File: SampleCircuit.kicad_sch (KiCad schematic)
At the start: 36 parts, among them J1 24V INPUT, J2 12V TEST, J3 5V TEST, J4 3.3V TEST, J5 SPEAKER, U1 LMZM23601SILR, U2 ESP32-S3-WROOM-1, U5 LMZM23601SILR, U5 NS4168, U6 LMZM23601SILR, U6 MicroSD

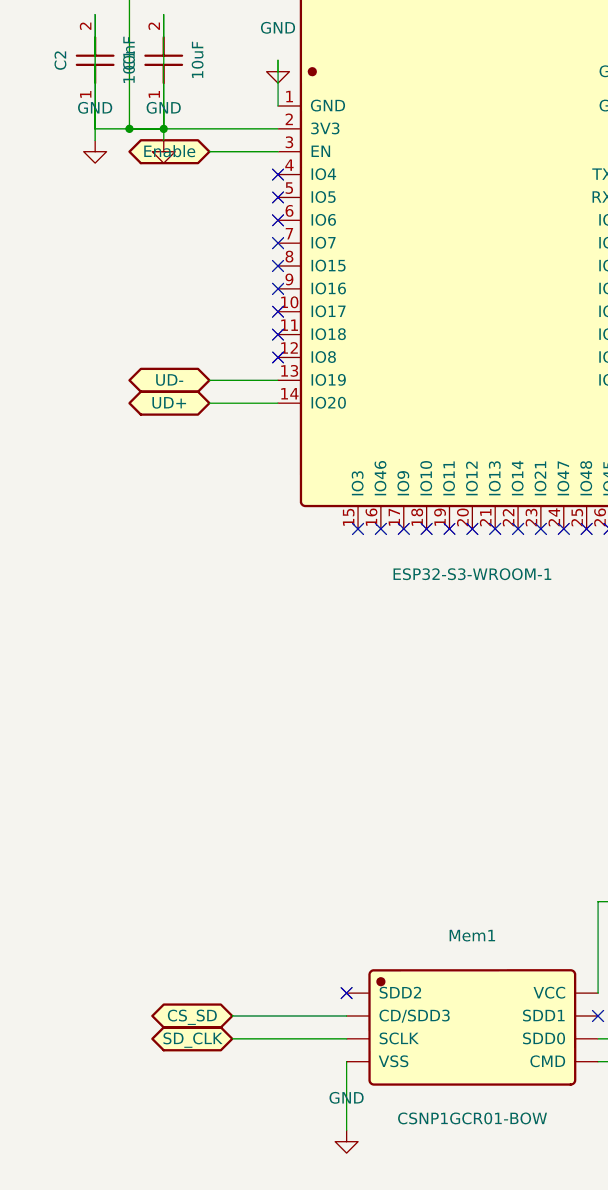
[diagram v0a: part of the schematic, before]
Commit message: Fix ESP32 GPIO wiring and flash chip select separation
- Add CS_FLASH port symbol to Ports.kicad_sym
- Map 9 ESP32 GPIO to ports: I2S (IO4-IO6), AMP_EN (IO7),
  SPI (IO15-IO18), CS_FLASH (IO8)
- Change flash template from CS_SD to CS_FLASH for separate
  chip select lines between flash and SD card
- Regenerate schematic with all signal connections verified

Co-Authored-By: Claude Opus 4.6 <noreply@anthropic.com>
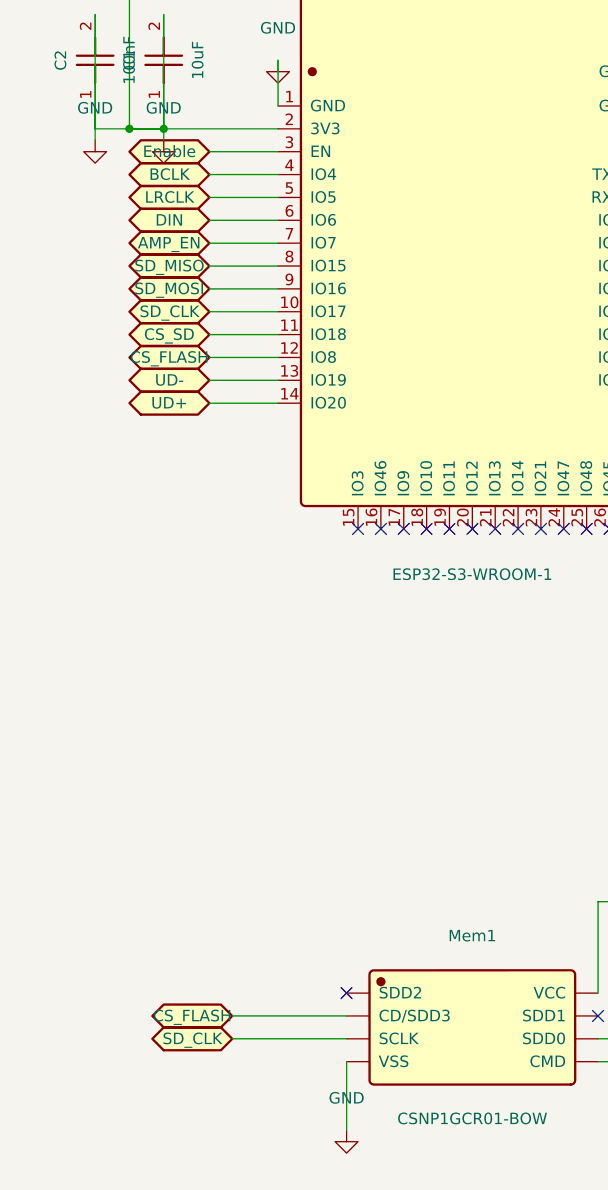
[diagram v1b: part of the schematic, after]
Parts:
- removed C2 (x2): 100nF, JLCImport:CC0805KRX7R9BB104, symbol JLCImport:CC0805KRX7R9BB104
- added C2 (x2): 100nF, JLCImport:CC0805KRX7R9BB104, symbol JLCImport:CC0805KRX7R9BB104
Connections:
- net +3.3V: now also C2.1, C2.1, C2.2, C2.2
- no-connect marks 48 -> 39

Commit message: Add TLV803S supervisor and RV-3028 RTC via patch system
Patched in supervisor_tlv803s (power-good/reset for ESP32 EN) and
rtc_rv3028 (I2C RTC with pull-ups, battery backup). Also includes
manual KiCad edits fixing ESP32 3V3 power wiring.

Co-Authored-By: Claude Opus 4.6 <noreply@anthropic.com>
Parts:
- added B3: CR1220, JLCImport:CR2032-BS-2-1, symbol JLCImport:CR2032-BS-2-1
- added C104, C39, C94: 100nF, JLCImport:CC0805KRX7R9BB104, symbol JLCImport:CC0805KRX7R9BB104
- added C93: 10uF, JLCImport:GRM32ER7YA106KA12L, symbol JLCImport:GRM32ER7YA106KA12L
- added R48, R89: 10k, JLCImport:0805W8F1002T5E, symbol JLCImport:0805W8F1002T5E
- added R94: 1k, JLCImport:0805W8F1001T5E, symbol JLCImport:0805W8F1001T5E
- added U15: TLV803S, JLCImport:TLV803SDBZR, symbol JLCImport:TLV803SDBZR
- added U23: RV-3028-C7, JLCImport:RV-3028-C7_32_768KHZ_1PPM_TA_QC, symbol JLCImport:RV-3028-C7_32_768KHZ_1PPM_TA_QC
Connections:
- net +3.3V: now also C39.1, C93.1, R48.1, U15.3 (VDD), U23.7 (VDD); no longer C1.1, C1.2, C1.2, C11.1, C11.2, C17.2, C18.2, C2.1, C2.2, C2.2, C3.1, C31.1, C32.1, C33.1, C34.1, C35.1, J1.2, J2.2, J3.2, J4.2, Mem1.4 (VSS), R2.2, R20.1, R32.2, R4.2, U1.1 (GND), U1.11 (EP), U1.2 (MODE/SYNC), U2.1 (GND), U2.40 (GND), U2.41 (GND), U5.1 (GND), U5.11 (EP), U5.2 (MODE/SYNC), U5.7 (GND), U5.9 (EP), U6.1 (GND), U6.11 (EP), U6.2 (MODE/SYNC), U6.6 (VSS), U6.9 (SHIELD)
- net GND: now reaches U6.7 (DAT0)
- net GND: now also C1.1, C1.2, C1.2, C11.1, C11.2, C17.2, C18.2, C2.1, C2.2, C2.2, C3.1, C31.1, C32.1, C33.1, C34.1, C35.1, J1.2, J2.2, J3.2, J4.2, Mem1.4 (VSS), R2.2, R20.1, R32.2, R4.2, U1.1 (GND), U1.11 (EP), U1.2 (MODE/SYNC), U2.1 (GND), U2.40 (GND), U2.41 (GND), U5.1 (GND), U5.11 (EP), U5.2 (MODE/SYNC), U5.7 (GND), U5.9 (EP), U6.1 (GND), U6.11 (EP), U6.2 (MODE/SYNC), U6.6 (VSS), U6.9 (SHIELD), B3.2, C104.1, C39.2, C93.2, C94.2, R89.2, U15.1 (GND), U23.5 (VSS)
- new net: B3.1, R94.2
- new net: C94.1, R48.2, U15.2 (RESET#)
- new net: R89.1, U23.8 (EVI)
- new net: C104.2, R94.1, U23.6 (VBACKUP)
- no-connect marks 39 -> 41
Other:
- moved on the sheet: C1, C11, C17, C18, C2, C3, C31, C32, C33, C34, C35, D8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

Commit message: Fix port symbols: pin passive → power_in for global net connectivity
All Ports:* symbols (Enable, SCL, SDA, BCLK, DIN, LRCLK, OUTP, OUTN,
etc.) had pin type 'passive' which prevented KiCad from forming global
nets. Changed to 'power_in' so matching port symbols connect automatically.

Co-Authored-By: Claude Opus 4.6 <noreply@anthropic.com>
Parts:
- renumbered C1 to C4, C2 to C5
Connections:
- net +3.3V: no longer C11.2
- net GND: now also Mem1.6 (SDD0), U2.8 (IO15); no longer C11.1
- net SD_CLK: now reaches U2.10 (IO17)
- net SD_CLK: now also Mem1.3 (SCLK), U6.5 (CLK)
- net CS_SD: now reaches U2.11 (IO18)
- net CS_SD: now also U6.2 (DAT3/CD)
- net CS_FLASH: now reaches U2.12 (IO8)
- net CS_FLASH: now also Mem1.2 (CD/SDD3)
- net UD-: now reaches U2.13 (IO19)
- net UD+: now reaches U2.14 (IO20)
- net Enable: now reaches U2.3 (EN)
- net Enable: now also C94.1, R48.2, U15.2 (RESET#)
- net RX: now reaches U2.36 (RXD0)
- net TX: now reaches U2.37 (TXD0)
- net BCLK: now reaches U2.4 (IO4)
- net BCLK: now also U5.3 (BCLK)
- net LRCLK: now reaches U2.5 (IO5)
- net LRCLK: now also U5.2 (LRCLK)
- net DIN: now reaches U2.6 (IO6)
- net DIN: now also U5.4 (SDATA)
- net AMP_EN: now reaches U2.7 (IO7)
- net AMP_EN: now also R20.2, U5.1 (CTRL)
- net SD_MOSI: now reaches U2.9 (IO16)
- net SD_MOSI: now also Mem1.5 (CMD), U6.3 (CMD)
- net SCL: now reaches U23.3 (SCL)
- net SDA: now reaches U23.4 (SDA)
- net OUTN: now reaches U5.5 (VON)
- net OUTN: now also J5.1
- net OUTP: now reaches U5.8 (VOP)
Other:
- moved on the sheet: B3, C104, C11, J3, J5, R89, R94, U23
